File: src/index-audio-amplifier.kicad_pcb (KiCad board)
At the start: 2 copper layers, 23.5 x 23.5 mm, 63 parts, among them J1 CU3616SASCLA004-LF, J2 SWD_PicoprobeCandybar, J3 Conn_01x02, J4 Conn_01x02, U1 RP2040, U2 NCP167, U3 W25Q16JVUXIQ, U4 MAX98360CENL, U5 NCP167, U6 MAX98360CENL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

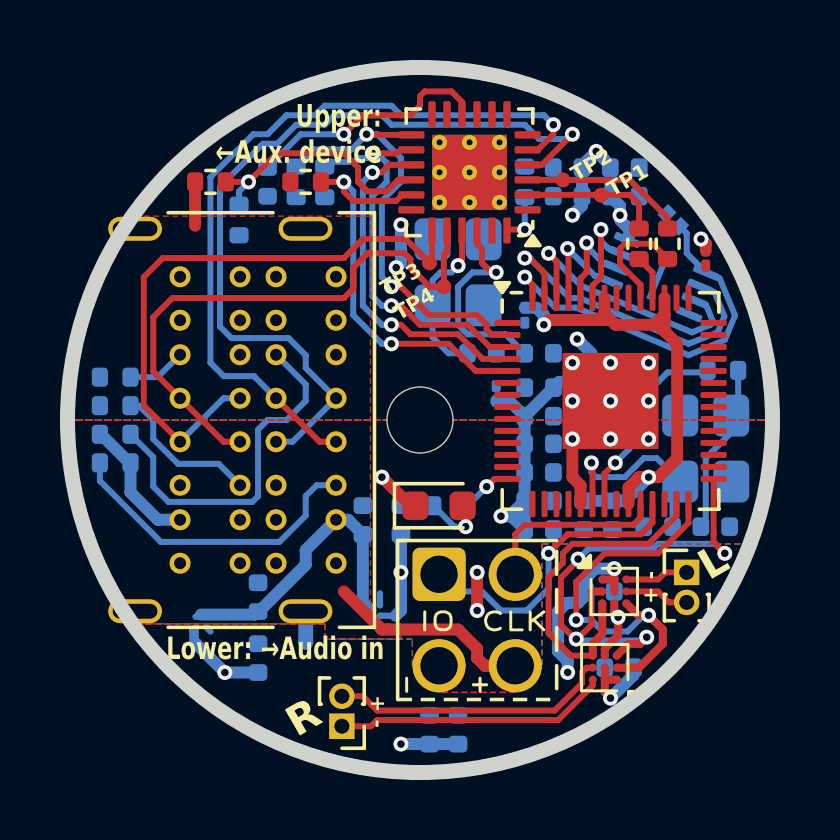
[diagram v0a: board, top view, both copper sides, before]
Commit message: Replace NCP167 with NCP187
NCP187 lets us output 4.2V to our amplifiers with SNS feedback.
<https://www.onsemi.com/download/data-sheet/pdf/ncp187-d.pdf>

Per the amplifiers' datasheet, this increased VDD will reduce THD+N.
<https://www.analog.com/media/en/technical-documentation/data-sheets/max98360a-max98360d.pdf>

We choose 4.2V output because we can expect a minimum of 4.5V to be
delivered to the board per the USB 2.0 specification, and the NCP187
has a maximum dropout of 220mV.  4.5V - 220mV = 4.28V, so 4.2 it is.
<https://www.usb.org/document-library/usb-20-specification>

Setting the MAX98360 gains to 6dB should yield a peak voltage output of
3.67V, which is well within range of our 4.2V output.  This results in
up to 1.125W sent to each 6ohm speaker, which is within the 2W power
handling of the Tectonic TEBM35C02-6B's found on the Index, and does not
exceed USB-2.0's 2.5W supply power when both speakers are powered at
full volume.
<https://cdn.prod.website-files.com/673cf5977476dddd8360dc22/67779956ffce5474ffe874a4_TEBM35C02-6B%20Datasheet.pdf>

We'll just have to see if 1.125W is enough for adequate volume levels...
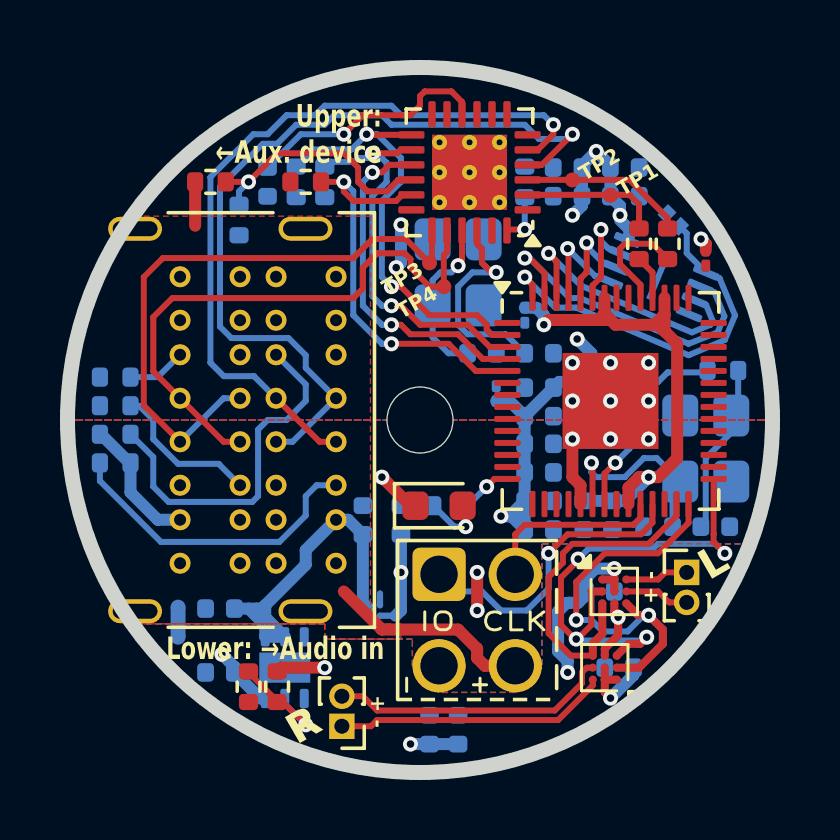
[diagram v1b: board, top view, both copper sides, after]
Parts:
- added R11: 330K, Resistor_SMD:R_0402_1005Metric, F.Cu at (143.7, 78.9)
- added R8: 90K, Resistor_SMD:R_0402_1005Metric, F.Cu at (142.8, 78.9)
- C102: value 1u -> 10u
- C19, C21: value 10u -> 100n
- C20, C22: value 100n -> 10u
- U5: value NCP167 -> NCP187AMT330TAG; footprint Package_CSP:WLCSP-4_0.64x0.64mm_Layout2x2_P0.35mm -> Package_DFN_QFN:DFN-6-1EP_2x2mm_P0.65mm_EP1.01x1.7mm
- moved C19 7.31 mm to (154.5, 75.7), turned to 0 degrees
- moved C20 7.31 mm to (148.8, 80.3), turned to 90 degrees
- moved NT1 4.26 mm to (140.4, 76.7)
- moved U5 3.18 mm to (144.0, 78.3)
- moved C102 1.36 mm to (141.8, 78.4), turned to 180 degrees
- moved C101 1.33 mm to (141.8, 76.3), turned to 180 degrees
- moved TP2 0.32 mm to (153.6, 62.0), turned to 30 degrees
- moved TP1 0.32 mm to (154.8, 62.5), turned to 30 degrees
- turned TP3 to 30 degrees
- turned TP4 to 30 degrees
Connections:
- C102 pad 1: +3V3A -> +4V2A
- C19 pad 1: +3V3A -> +4V2A
- C20 pad 1: +3V3A -> +4V2A
- C21 pad 1: +3V3A -> +4V2A
- C22 pad 1: +3V3A -> +4V2A
- U4 pad A1: +3V3A -> +4V2A
- U4 pad A2: +3V3A -> +4V2A
- U4 pad B2: +3V3A -> +4V2A
- U6 pad A1: +3V3A -> +4V2A
- U6 pad A2: +3V3A -> +4V2A
- U6 pad B2: +3V3A -> +4V2A
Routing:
- net +3V3A: track 14.5 -> 0.00 mm, vias 5 -> 0
- net +4V2A: track 0.00 -> 12.7 mm, vias 0 -> 5
- net Net-(U5-SNS): track 0.00 -> 3.85 mm, vias 0 -> 1
- net VBUS: track 23.6 -> 25.9 mm
- net AGND: track 2.18 -> 3.62 mm, vias 1 -> 2
- added copper zone on F.Cu, net +4V2A
- removed copper zone on F.Cu, net +3V3A
